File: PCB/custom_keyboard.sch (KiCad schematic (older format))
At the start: 397 parts, among them IC1 FE2.1, J1 USB_A, J2 USB_A, J3 USB_A, J4 Conn_01x08_Male, SW1 SW_Push, U1 PRTR5V0U2X, U2 24LC02, U3 PRTR5V0U2X, U4 PRTR5V0U2X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

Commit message: Halfway done USB ports
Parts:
- removed TP1, TP2, TP3, TP4: VCC, TestPoint:TestPoint_Pad_D1.0mm, symbol Connector:TestPoint
- IC1: footprint FE2.1:LQFP-48_L7.0-W7.0-P0.50-LS9.0-BL -> custom-footprints:FE2.1
- U2: footprint Package_TO_SOT_SMD:SOT-23-8 -> custom-footprints:24LC04
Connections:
- wire segments 2363 -> 2355
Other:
- moved on the sheet: R41, R42, R43, R44, R45, R46
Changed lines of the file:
@@
 Wire Notes Line
 	9100 18200 11650 18200
-$Comp
-L Connector:TestPoint TP1
-U 1 1 A8CE47BF
-P 16550 11650
-F 0 "TP1" V 16745 11722 50  0000 C CNN
-F 1 "VCC" V 16654 11722 50  0000 C CNN
-F 2 "TestPoint:TestPoint_Pad_D1.0mm" H 16750 11650 50  0001 C CNN
-F 3 "~" H 16750 11650 50  0001 C CNN
-	1    16550 11650
-	0    -1   -1   0
-$EndComp
 Connection ~ 16700 11900
 Wire Wire Line
@@
 F 0 "U2" H 19800 11850 50  0000 C CNN
 F 1 "24LC02" H 19800 11750 50  0000 C CNN
-F 2 "Package_TO_SOT_SMD:SOT-23-8" H 19450 12100 50  0001 C CNN
+F 2 "custom-footprints:24LC04" H 19450 12100 50  0001 C CNN
 F 3 "http://ww1.microchip.com/downloads/en/DeviceDoc/21709c.pdf" H 19450 12100 50  0001 C CNN
 	1    19450 12100
@@
 F 0 "IC1" H 17750 15900 60  0000 L CNN
 F 1 "FE2.1" H 17700 15800 60  0000 L CNN
-F 2 "FE2.1:LQFP-48_L7.0-W7.0-P0.50-LS9.0-BL" H 14100 16900 60  0001 C CNN
+F 2 "custom-footprints:FE2.1" H 14100 16900 60  0001 C CNN
 F 3 "" H 14100 16900 60  0000 C CNN
 	1    16800 16750
@@
 	16800 12900 16800 11800
 Wire Wire Line
-	16700 11600 16700 11650
-Wire Wire Line
-	16550 11650 16700 11650
-Connection ~ 16700 11650
-Wire Wire Line
-	16700 11650 16700 11900
-Wire Wire Line
 	16150 11700 16150 11800
 Wire Wire Line
@@
 	25800 18150 25800 18250
 Wire Wire Line
-	25250 18100 25250 18350
-Connection ~ 25250 18100
-Wire Wire Line
-	25400 18100 25250 18100
-Wire Wire Line
-	25250 18050 25250 18100
-Wire Wire Line
 	25150 19350 25150 18250
 Wire Wire Line
@@
 	25250 19250 25050 19250
 Connection ~ 25250 18350
-$Comp
-L Connector:TestPoint TP4
-U 1 1 EFE7B0A7
-P 25400 18100
-F 0 "TP4" V 25595 18172 50  0000 C CNN
-F 1 "VCC" V 25504 18172 50  0000 C CNN
-F 2 "TestPoint:TestPoint_Pad_D1.0mm" H 25600 18100 50  0001 C CNN
-F 3 "~" H 25600 18100 50  0001 C CNN
-	1    25400 18100
-	0    1    -1   0
-$EndComp
 Wire Wire Line
 	25800 16250 25050 16250
@@
 	25800 16250 25800 16350
 Wire Wire Line
-	25250 16200 25250 16450
-Connection ~ 25250 16200
-Wire Wire Line
-	25400 16200 25250 16200
-Wire Wire Line
-	25250 16150 25250 16200
-Wire Wire Line
 	25150 17450 25150 16350
 Wire Wire Line
@@
 	25250 17350 25050 17350
 Connection ~ 25250 16450
-$Comp
-L Connector:TestPoint TP3
-U 1 1 EFACD50C
-P 25400 16200
-F 0 "TP3" V 25595 16272 50  0000 C CNN
-F 1 "VCC" V 25504 16272 50  0000 C CNN
-F 2 "TestPoint:TestPoint_Pad_D1.0mm" H 25600 16200 50  0001 C CNN
-F 3 "~" H 25600 16200 50  0001 C CNN
-	1    25400 16200
-	0    1    -1   0
-$EndComp
 Wire Wire Line
 	25800 14350 25050 14350
@@
 	25800 14350 25800 14450
 Wire Wire Line
-	25250 14300 25250 14550
-Connection ~ 25250 14300
-Wire Wire Line
-	25400 14300 25250 14300
-Wire Wire Line
-	25250 14250 25250 14300
-Wire Wire Line
 	25150 15550 25150 14450
 Wire Wire Line
@@
 	25250 15450 25050 15450
 Connection ~ 25250 14550
-$Comp
-L Connector:TestPoint TP2
-U 1 1 EE8C51FC
-P 25400 14300
-F 0 "TP2" V 25595 14372 50  0000 C CNN
-F 1 "VCC" V 25504 14372 50  0000 C CNN
-F 2 "TestPoint:TestPoint_Pad_D1.0mm" H 25600 14300 50  0001 C CNN
-F 3 "~" H 25600 14300 50  0001 C CNN
-	1    25400 14300
-	0    1    -1   0
-$EndComp
 Text GLabel 27300 18950 2    50   Input ~ 0
 HUB_PORT7_D-
@@
 $EndComp
 Wire Wire Line
-	21500 19050 21500 19250
-Connection ~ 21500 19250
-Wire Wire Line
-	21200 19250 21500 19250
-Wire Wire Line
-	21500 19250 22300 19250
-Wire Wire Line
-	22200 19050 22200 19150
-Connection ~ 22200 19150
-Wire Wire Line
-	21200 19150 22200 19150
-Wire Wire Line
-	22200 19150 22300 19150
-Wire Wire Line
 	22100 19050 22200 19050
 Wire Wire Line
@@
 $EndComp
 Wire Wire Line
-	22600 19250 22500 19250
-Wire Wire Line
-	22500 19150 22600 19150
-Wire Wire Line
 	20900 19550 20900 19850
 Wire Wire Line
@@
 L Device:R_Small R45
 U 1 1 DF22507D
-P 22400 19150
-F 0 "R45" V 22600 19150 50  0000 C CNN
-F 1 "22" V 22500 19150 50  0000 C CNN
-F 2 "Resistor_SMD:R_0805_2012Metric" H 22400 19150 50  0001 C CNN
-F 3 "~" H 22400 19150 50  0001 C CNN
-	1    22400 19150
+P 21350 19150
+F 0 "R45" V 21550 19150 50  0000 C CNN
+F 1 "22" V 21450 19150 50  0000 C CNN
+F 2 "Resistor_SMD:R_0805_2012Metric" H 21350 19150 50  0001 C CNN
+F 3 "~" H 21350 19150 50  0001 C CNN
+	1    21350 19150
 	0    -1   -1   0
 $EndComp
@@
 L Device:R_Small R46
 U 1 1 DF225073
-P 22400 19250
-F 0 "R46" V 22300 19250 50  0000 C CNN
-F 1 "22" V 22200 19250 50  0000 C CNN
-F 2 "Resistor_SMD:R_0805_2012Metric" H 22400 19250 50  0001 C CNN
-F 3 "~" H 22400 19250 50  0001 C CNN
-	1    22400 19250
+P 21350 19250
+F 0 "R46" V 21250 19250 50  0000 C CNN
+F 1 "22" V 21150 19250 50  0000 C CNN
+F 2 "Resistor_SMD:R_0805_2012Metric" H 21350 19250 50  0001 C CNN
+F 3 "~" H 21350 19250 50  0001 C CNN
+	1    21350 19250
 	0    -1   -1   0
 $EndComp
@@
 $EndComp
 Wire Wire Line
-	22600 17250 22500 17250
-Wire Wire Line
-	22500 17150 22600 17150
-Wire Wire Line
 	20900 17550 20900 17850
 Wire Wire Line
@@
 L Device:R_Small R43
 U 1 1 DEEC6E16
-P 22400 17150
-F 0 "R43" V 22600 17150 50  0000 C CNN
-F 1 "22" V 22500 17150 50  0000 C CNN
-F 2 "Resistor_SMD:R_0805_2012Metric" H 22400 17150 50  0001 C CNN
-F 3 "~" H 22400 17150 50  0001 C CNN
-	1    22400 17150
+P 21350 17150
+F 0 "R43" V 21550 17150 50  0000 C CNN
+F 1 "22" V 21450 17150 50  0000 C CNN
+F 2 "Resistor_SMD:R_0805_2012Metric" H 21350 17150 50  0001 C CNN
+F 3 "~" H 21350 17150 50  0001 C CNN
+	1    21350 17150
 	0    -1   -1   0
 $EndComp
@@
 L Device:R_Small R44
 U 1 1 DEEC6E0C
-P 22400 17250
-F 0 "R44" V 22300 17250 50  0000 C CNN
-F 1 "22" V 22200 17250 50  0000 C CNN
-F 2 "Resistor_SMD:R_0805_2012Metric" H 22400 17250 50  0001 C CNN
-F 3 "~" H 22400 17250 50  0001 C CNN
-	1    22400 17250
+P 21350 17250
+F 0 "R44" V 21250 17250 50  0000 C CNN
+F 1 "22" V 21150 17250 50  0000 C CNN
+F 2 "Resistor_SMD:R_0805_2012Metric" H 21350 17250 50  0001 C CNN
+F 3 "~" H 21350 17250 50  0001 C CNN
+	1    21350 17250
 	0    -1   -1   0
 $EndComp
-Text GLabel 22600 17250 2    50   Input ~ 0
+Text GLabel 22400 17250 2    50   Input ~ 0
 HUB_PORT3_D-
-Text GLabel 22600 17150 2    50   Input ~ 0
+Text GLabel 22400 17150 2    50   Input ~ 0
 HUB_PORT3_D+
 $Comp
@@
 $EndComp
 Wire Wire Line
-	21500 15000 21500 15200
-Connection ~ 21500 15200
-Wire Wire Line
-	21200 15200 21500 15200
-Wire Wire Line
-	21500 15200 22300 15200
-Wire Wire Line
-	22200 15000 22200 15100
-Connection ~ 22200 15100
-Wire Wire Line
-	21200 15100 22200 15100
-Wire Wire Line
-	22200 15100 22300 15100
-Wire Wire Line
 	22100 15000 22200 15000
 Wire Wire Line
@@
 $EndComp
 Wire Wire Line
-	22600 15200 22500 15200
-Wire Wire Line
-	22500 15100 22600 15100
-Wire Wire Line
 	20900 15500 20900 15800
 Wire Wire Line
@@
 	1    0    0    -1
 $EndComp
-$Comp
-L Device:R_Small R41
-U 1 1 BA600C31
-P 22400 15100
-F 0 "R41" V 22600 15100 50  0000 C CNN
-F 1 "22" V 22500 15100 50  0000 C CNN
-F 2 "Resistor_SMD:R_0805_2012Metric" H 22400 15100 50  0001 C CNN
-F 3 "~" H 22400 15100 50  0001 C CNN
-	1    22400 15100
-	0    -1   -1   0
-$EndComp
-$Comp
-L Device:R_Small R42
-U 1 1 BA6000FA
-P 22400 15200
-F 0 "R42" V 22300 15200 50  0000 C CNN
-F 1 "22" V 22200 15200 50  0000 C CNN
-F 2 "Resistor_SMD:R_0805_2012Metric" H 22400 15200 50  0001 C CNN
-F 3 "~" H 22400 15200 50  0001 C CNN
-	1    22400 15200
-	0    -1   -1   0
-$EndComp
-Text GLabel 22600 15200 2    50   Input ~ 0
+Text GLabel 22400 15200 2    50   Input ~ 0
 HUB_PORT2_D-
-Text GLabel 22600 15100 2    50   Input ~ 0
+Text GLabel 22400 15100 2    50   Input ~ 0
 HUB_PORT2_D+
 $Comp
@@
 Text Notes 13900 3550 0    315  ~ 0
 7
-Text Notes 12350 3550 0    315  ~ 0
+Text Notes 12400 3550 0    315  ~ 0
 6
 Text Notes 11000 3550 0    315  ~ 0
 5
-Text Notes 9550 3550 0    315  ~ 0
+Text Notes 9600 3550 0    315  ~ 0
 4
 Text Notes 8300 3550 0    315  ~ 0
@@
 	0    1    -1   0
 $EndComp
+$Comp
+L Device:R_Small R41
+U 1 1 BA600C31
+P 21350 15100
+F 0 "R41" V 21550 15100 50  0000 C CNN
+F 1 "22" V 21450 15100 50  0000 C CNN
+F 2 "Resistor_SMD:R_0805_2012Metric" H 21350 15100 50  0001 C CNN
+F 3 "~" H 21350 15100 50  0001 C CNN
+	1    21350 15100
+	0    -1   -1   0
+$EndComp
+$Comp
+L Device:R_Small R42
+U 1 1 BA6000FA
+P 21350 15200
+F 0 "R42" V 21250 15200 50  0000 C CNN
+F 1 "22" V 21150 15200 50  0000 C CNN
+F 2 "Resistor_SMD:R_0805_2012Metric" H 21350 15200 50  0001 C CNN
+F 3 "~" H 21350 15200 50  0001 C CNN
+	1    21350 15200
+	0    -1   -1   0
+$EndComp
 Wire Wire Line
-	21200 17250 22200 17250
+	21200 15100 21250 15100
 Wire Wire Line
-	21200 17150 21500 17150
+	21200 15200 21250 15200
 Wire Wire Line
-	22200 17050 22200 17250
-Connection ~ 22200 17250
+	21450 15200 22200 15200
+Wire Wire Line
+	21450 15100 21500 15100
+Wire Wire Line
+	22200 15000 22200 15200
+Connection ~ 22200 15200
 Wire Wire Line
-	22200 17250 22300 17250
+	22200 15200 22400 15200
+Wire Wire Line
+	21500 15000 21500 15100
+Connection ~ 21500 15100
+Wire Wire Line
+	21500 15100 22400 15100
+Wire Wire Line
+	22200 17050 22200 17250
 Wire Wire Line
 	21500 17050 21500 17150
+Wire Wire Line
+	22200 17250 22400 17250
+Wire Wire Line
+	21500 17150 22400 17150
+Wire Wire Line
+	21200 17150 21250 17150
+Wire Wire Line
+	21200 17250 21250 17250
+Wire Wire Line
+	21450 17250 22200 17250
+Connection ~ 22200 17250
+Wire Wire Line
+	21450 17150 21500 17150
 Connection ~ 21500 17150
 Wire Wire Line
-	21500 17150 22300 17150
+	21200 19150 21250 19150
+Wire Wire Line
+	21450 19150 21500 19150
+Wire Wire Line
+	21450 19250 22200 19250
+Wire Wire Line
+	21250 19250 21200 19250
+Wire Wire Line
+	21500 19050 21500 19150
+Connection ~ 21500 19150
+Wire Wire Line
+	21500 19150 22600 19150
+Wire Wire Line
+	22200 19050 22200 19250
+Connection ~ 22200 19250
+Wire Wire Line
+	22200 19250 22600 19250
+Wire Wire Line
+	16700 11600 16700 11900
+Wire Wire Line
+	25250 14250 25250 14550
+Wire Wire Line
+	25250 16150 25250 16450
+Wire Wire Line
+	25250 18050 25250 18350
 $EndSCHEMATC

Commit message: Routed lights
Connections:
- net +5V: no longer MX70.5 (DOUT), MX74.4 (DIN)
- new net: MX70.5 (DOUT), MX74.4 (DIN)
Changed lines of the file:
@@
 Wire Wire Line
 	10600 3900 10500 3900
-Connection ~ 23800 4100
-Wire Wire Line
-	23800 4100 23200 4100
 Wire Wire Line
 	20400 6600 20300 6600

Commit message: Organized USB Hub location
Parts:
- added F1: 4A, Fuse:Fuse_1206_3216Metric, symbol Device:Fuse_Small
- added FB1, FB2, FB3, FB4, FB5, FB6, FB7: 3A, Inductor_SMD:L_0805_2012Metric, symbol Device:Ferrite_Bead_Small
- added R13: 4.7k, Resistor_SMD:R_0805_2012Metric, symbol Device:R_Small
- added R24: 1M, Resistor_SMD:R_0805_2012Metric, symbol Device:R_Small
- C40: value 4.7uF -> 0.1uF
- C42: value 100nF -> 0.1uF
- C53, C54: value 22pF -> 20pF
- R11: value 100k -> 4.7k
- R15: value 47k -> 4.7k
- renumbered R13 to R52, R24 to R53
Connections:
- net +3V3: now also C40.1, C42.1, R11.1, R12.1, R15.1, R13.1; no longer R12.2, U2.7 (WP)
- net +5V: now also IC1.41 (VBUSM), F1.1, FB2.2, FB4.2, FB6.2; no longer C40.2, C42.2, J1.1 (VBUS), J2.1 (VBUS), J3.1 (VBUS), R15.1, U6.4 (VCC), U7.4 (VCC), U8.4 (VCC), USB1.11 (VBUS), USB1.2 (VBUS)
- net COL0: now also U9.44 (PA7); no longer U9.47 (PA4)
- net COL1: now also U9.45 (PA6); no longer U9.46 (PA5)
- net COL10: now also U9.41 (PC6); no longer U9.36 (PC1)
- net COL11: now also U9.42 (PC7); no longer U9.35 (PC0)
- net COL12: now also U9.33 (PE0); no longer U9.34 (PE1)
- net COL13: now also U9.34 (PE1); no longer U9.33 (PE0)
- net COL14: now also U9.31 (PD6); no longer U9.32 (PD7)
- net COL15: now also U9.32 (PD7); no longer U9.31 (PD6)
- net COL16: now also U9.29 (PD4); no longer U9.30 (PD5)
- net COL17: now also U9.30 (PD5); no longer U9.29 (PD4)
- net COL2: now also U9.46 (PA5); no longer U9.45 (PA6)
- net COL3: now also U9.47 (PA4); no longer U9.44 (PA7)
- net COL4: now also U9.35 (PC0); no longer U9.42 (PC7)
- net COL5: now also U9.36 (PC1); no longer U9.41 (PC6)
- net COL6: now also U9.37 (PC2); no longer U9.40 (PC5)
- net COL7: now also U9.38 (PC3); no longer U9.39 (PC4)
- net COL8: now also U9.39 (PC4); no longer U9.38 (PC3)
- net COL9: now also U9.40 (PC5); no longer U9.37 (PC2)
- net GND: now also C40.2, C42.2, FB3.1, FB5.1, FB7.1; no longer J1.4 (GND), J2.4 (GND), J3.4 (GND)
- net HUB_LED1: now also R13.2
- net HUB_PORT2_D+: no longer U6.3 (IO2)
- net HUB_PORT2_D-: no longer U6.2 (IO1)
- net HUB_PORT3_D+: no longer U7.3 (IO2)
- net HUB_PORT3_D-: no longer U7.2 (IO1)
- net HUB_PORT4_D+: no longer U8.3 (IO2)
- net HUB_PORT4_D-: no longer U8.2 (IO1)
- net HUB_SDA: now also R15.2
- net HUB_XIN: now also R24.1
- net HUB_XOUT: now also R24.2
- net ROT1_ROW: now also U9.61 (PF0); no longer U9.56 (PF5)
- net ROW1: now also U9.60 (PF1); no longer U9.57 (PF4)
- net ROW2: now also U9.59 (PF2); no longer U9.58 (PF3)
- net ROW3: now also U9.58 (PF3); no longer U9.59 (PF2)
- net ROW4: now also U9.57 (PF4); no longer U9.60 (PF1)
- net ROW5: now also U9.56 (PF5); no longer U9.61 (PF0)
- net at IC1.40 (XRSTJ): now also R12.2; no longer R12.1
- net at J1.2 (D-), R42.1: now also U6.3 (IO2)
- net at J1.3 (D+), R41.1: now also U6.2 (IO1)
- net at J2.2 (D-), R44.1: now also U7.3 (IO2)
- net at J2.3 (D+), R43.1: now also U7.2 (IO1)
- net at J3.2 (D-), R46.1: now also U8.3 (IO2)
- net at J3.3 (D+), R45.1: now also U8.2 (IO1)
- new net: FB1.1, USB1.11 (VBUS), USB1.2 (VBUS)
- new net: R11.2, U2.7 (WP)
- new net: FB3.2, J1.4 (GND)
- new net: FB5.2, J2.4 (GND)
- new net: FB7.2, J3.4 (GND)
- new net: FB2.1, J1.1 (VBUS), U6.4 (VCC)
- new net: FB4.1, J2.1 (VBUS), U7.4 (VCC)
- new net: FB6.1, J3.1 (VBUS), U8.4 (VCC)
- new net VCC: F1.2, FB1.2
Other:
- moved on the sheet: C117, C118, C119, C120, C41, C53, C54, R1, R12, R14, R16, R2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

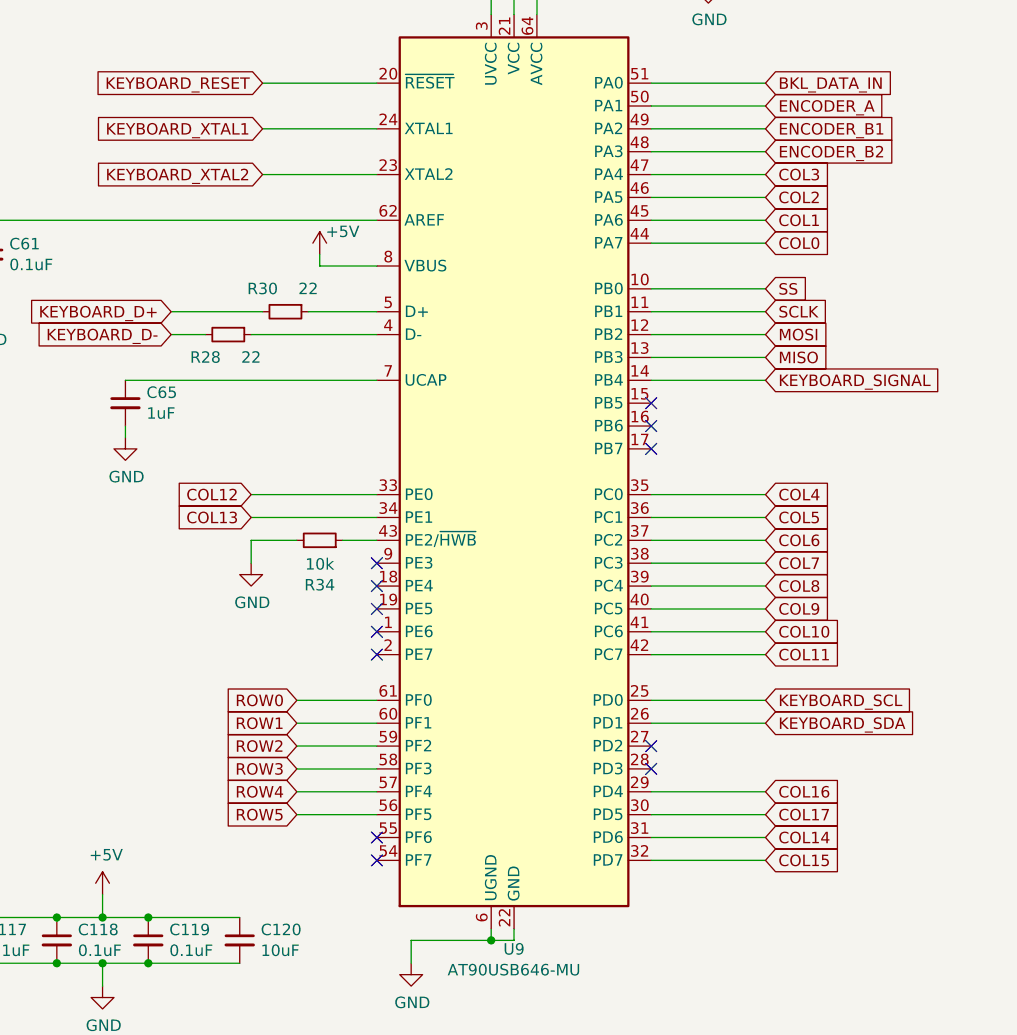
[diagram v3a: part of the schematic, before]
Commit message: Connected controller to columns
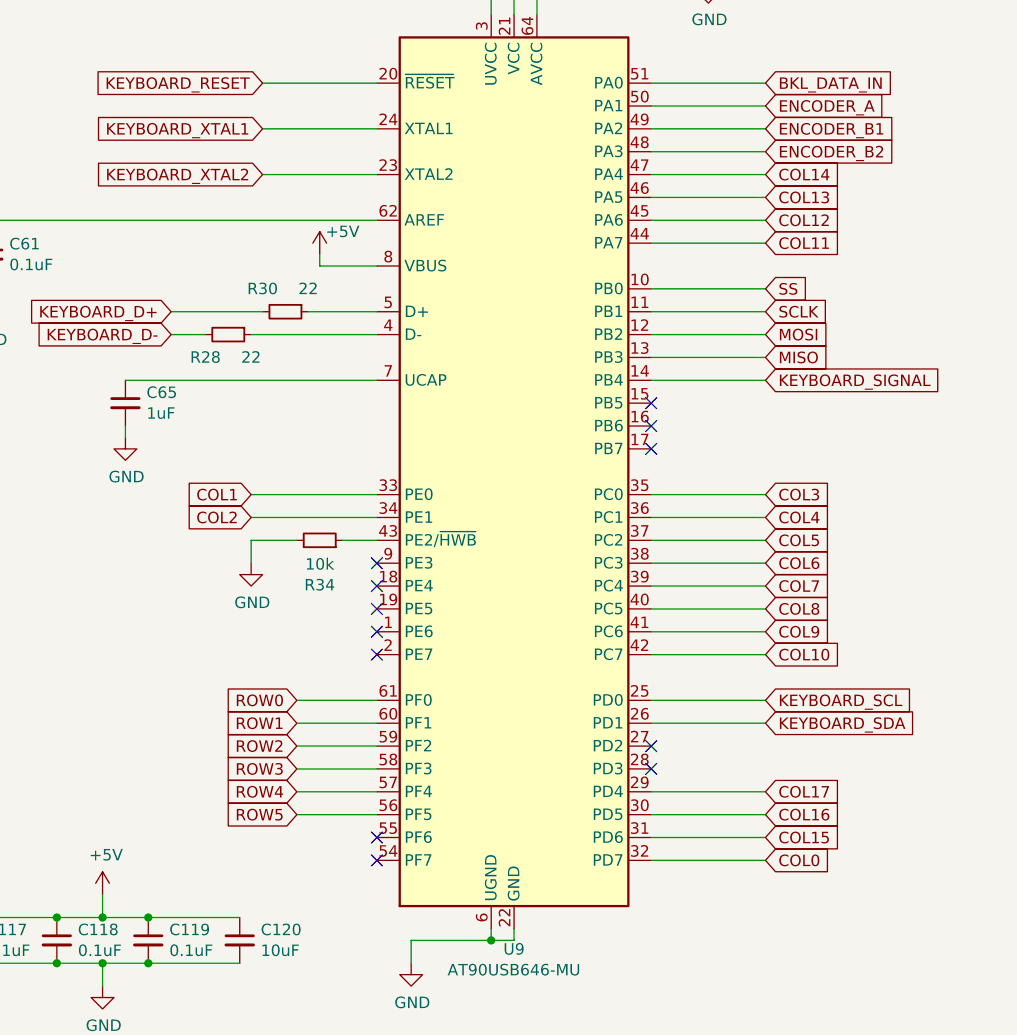
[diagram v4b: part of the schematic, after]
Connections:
- net COL0: now also U9.32 (PD7); no longer U9.44 (PA7)
- net COL1: now also U9.33 (PE0); no longer U9.45 (PA6)
- net COL10: now also U9.42 (PC7); no longer U9.41 (PC6)
- net COL11: now also U9.44 (PA7); no longer U9.42 (PC7)
- net COL12: now also U9.45 (PA6); no longer U9.33 (PE0)
- net COL13: now also U9.46 (PA5); no longer U9.34 (PE1)
- net COL14: now also U9.47 (PA4); no longer U9.31 (PD6)
- net COL15: now also U9.31 (PD6); no longer U9.32 (PD7)
- net COL16: now also U9.30 (PD5); no longer U9.29 (PD4)
- net COL17: now also U9.29 (PD4); no longer U9.30 (PD5)
- net COL2: now also U9.34 (PE1); no longer U9.46 (PA5)
- net COL3: now also U9.35 (PC0); no longer U9.47 (PA4)
- net COL4: now also U9.36 (PC1); no longer U9.35 (PC0)
- net COL5: now also U9.37 (PC2); no longer U9.36 (PC1)
- net COL6: now also U9.38 (PC3); no longer U9.37 (PC2)
- net COL7: now also U9.39 (PC4); no longer U9.38 (PC3)
- net COL8: now also U9.40 (PC5); no longer U9.39 (PC4)
- net COL9: now also U9.41 (PC6); no longer U9.40 (PC5)
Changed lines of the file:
@@
 Wire Wire Line
 	7200 15850 7700 15850
-Text GLabel 7700 19050 2    50   Input ~ 0
-COL17
 Text GLabel 7700 18950 2    50   Input ~ 0
+COL17
+Text GLabel 7700 19050 2    50   Input ~ 0
 COL16
-Text GLabel 7700 19250 2    50   Input ~ 0
-COL15
 Text GLabel 7700 19150 2    50   Input ~ 0
+COL15
+Text GLabel 7700 16250 2    50   Input ~ 0
 COL14
 Wire Wire Line
@@
 Text GLabel 7700 16150 2    50   Input ~ 0
 ENCODER_B2
-Text GLabel 7700 16550 2    50   Input ~ 0
+Text GLabel 7700 19250 2    50   Input ~ 0
 COL0
-Text GLabel 7700 16450 2    50   Input ~ 0
+Text GLabel 5450 17650 0    50   Input ~ 0
 COL1
-Text GLabel 7700 16350 2    50   Input ~ 0
+Text GLabel 5450 17750 0    50   Input ~ 0
 COL2
-Text GLabel 7700 16250 2    50   Input ~ 0
+Text GLabel 7700 17650 2    50   Input ~ 0
 COL3
-Text GLabel 5450 17750 0    50   Input ~ 0
+Text GLabel 7700 16350 2    50   Input ~ 0
 COL13
-Text GLabel 5450 17650 0    50   Input ~ 0
+Text GLabel 7700 16450 2    50   Input ~ 0
 COL12
 $Comp
@@
 Wire Wire Line
 	16900 11600 17050 11600
-Text GLabel 7700 18350 2    50   Input ~ 0
+Text GLabel 7700 16550 2    50   Input ~ 0
 COL11
-Text GLabel 7700 18250 2    50   Input ~ 0
+Text GLabel 7700 18350 2    50   Input ~ 0
 COL10
-Text GLabel 7700 18150 2    50   Input ~ 0
+Text GLabel 7700 18250 2    50   Input ~ 0
 COL9
-Text GLabel 7700 18050 2    50   Input ~ 0
+Text GLabel 7700 18150 2    50   Input ~ 0
 COL8
-Text GLabel 7700 17950 2    50   Input ~ 0
+Text GLabel 7700 18050 2    50   Input ~ 0
 COL7
-Text GLabel 7700 17850 2    50   Input ~ 0
+Text GLabel 7700 17950 2    50   Input ~ 0
 COL6
-Text GLabel 7700 17750 2    50   Input ~ 0
+Text GLabel 7700 17850 2    50   Input ~ 0
 COL5
-Text GLabel 7700 17650 2    50   Input ~ 0
+Text GLabel 7700 17750 2    50   Input ~ 0
 COL4
 $EndSCHEMATC
